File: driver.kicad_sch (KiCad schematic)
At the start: 24 parts, among them U10 74AUC2G32, U11 SN74AUP2G08, U12 74AUC2G32, U13 SN74AUP2G08, U14 74AUC2G32, U15 SN74AUP2G08, U16 SN74AUP2G08, U17 SN74AUP2G08, U18 74AUC2G32, U19 74AUC2G32, U20 SN74AUP2G08, U21 74AUC2G32, U22 SN74AUP2G08, U23 74AUC2G32, U24 SN74AUP2G08, U25 74AUC2G32, U26 SN74AUP2G08, U27 74AUC2G32, U28 SN74AUP2G08, U29 74AUC2G32, U6 Inverter_Schmitt_Dual, U7 Inverter_Schmitt_Dual, U8 SN74AUP2G08, U9 74AUC2G32

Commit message: schem: fix logic error
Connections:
- net D1: now also U26.5
- net ~{D1}: no longer U26.5
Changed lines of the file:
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@@
+	)
+	(junction
+		(at 152.4 77.47)
+		(diameter 0)
+		(color 0 0 0 0)
 	)
 	(junction
@@
 	)
 	(junction
-		(at 156.21 104.14)
-		(diameter 0)
-		(color 0 0 0 0)
-	)
-	(junction
 		(at 26.67 73.66)
 		(diameter 0)
@@
 	(wire
 		(pts
-			(xy 156.21 104.14) (xy 156.21 116.84)
-		)
-		(stroke
-			(width 0)
-			(type default)
-		)
-	)
-	(wire
-		(pts
 			(xy 213.36 21.59) (xy 213.36 20.32)
 		)
@@
 	(wire
 		(pts
-			(xy 156.21 116.84) (xy 173.99 116.84)
-		)
-		(stroke
-			(width 0)
-			(type default)
-		)
-	)
-	(wire
-		(pts
 			(xy 73.66 140.97) (xy 72.39 140.97)
 		)
@@
 	(wire
 		(pts
+			(xy 152.4 77.47) (xy 152.4 116.84)
+		)
+		(stroke
+			(width 0)
+			(type default)
+		)
+	)
+	(wire
+		(pts
 			(xy 233.68 72.39) (xy 234.95 72.39)
 		)
@@
 		)
 		(stroke
+			(width 0)
+			(type default)
+		)
+	)
+	(wire
+		(pts
+			(xy 152.4 116.84) (xy 173.99 116.84)
+		)
+		(stroke

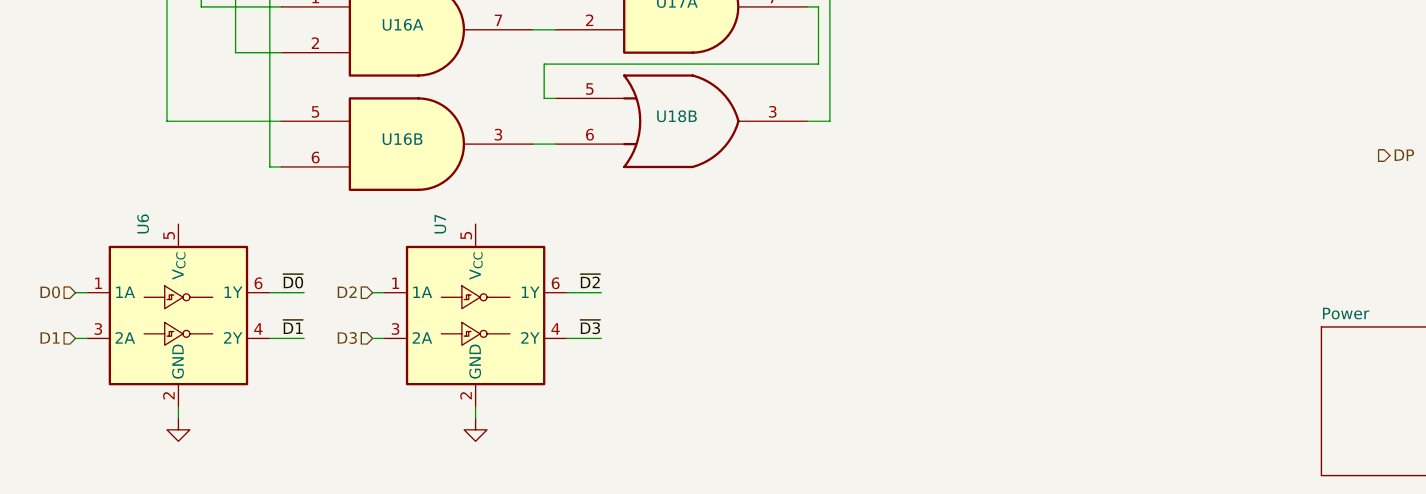
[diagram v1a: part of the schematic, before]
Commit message: schem: add inverters power
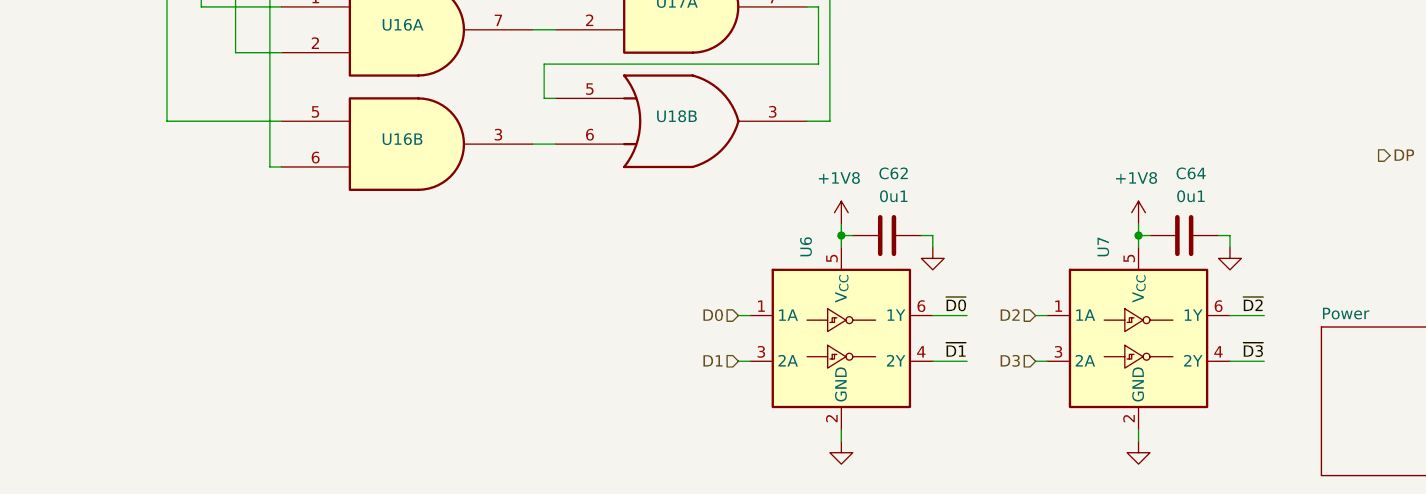
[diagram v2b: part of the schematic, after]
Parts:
- added C62, C64: 0u1, Capacitor_SMD:C_0402_1005Metric, symbol Device:C
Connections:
- net GND: now also C62.2, C64.2
- net +1V8: now reaches U6.5 (V_{CC})
- net +1V8: now also U7.5 (V_{CC}), C62.1, C64.1
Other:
- moved on the sheet: U6, U7

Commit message: schem: run and fix ERC
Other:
- moved on the sheet: U19A
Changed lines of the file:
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@@
 	)
 	(junction
-		(at 116.84 16.51)
-		(diameter 0)
-		(color 0 0 0 0)
-	)
-	(junction
 		(at 83.82 25.4)
 		(diameter 0)
@@
 	)
 	(no_connect
-		(at 144.78 19.05)
+		(at 146.05 19.05)
 	)
 	(no_connect
@@
 	(wire
 		(pts
+			(xy 118.11 16.51) (xy 116.84 16.51)
+		)
+		(stroke
+			(width 0)
+			(type default)
+		)
+	)
+	(wire
+		(pts
 			(xy 152.4 77.47) (xy 152.4 116.84)
 		)
@@
 	(wire
 		(pts
-			(xy 118.11 16.51) (xy 116.84 16.51)
-		)
-		(stroke
-			(width 0)
-			(type default)
-		)
-	)
-	(wire
-		(pts
 			(xy 105.41 168.91) (xy 105.41 170.18)
 		)
@@
 		)
 	)
-	(hierarchical_label "DP"
-		(shape output)
-		(at 165.1 160.02 0)
-		(effects
-			(font
-				(size 1.27 1.27)
-			)
-			(justify left)
-		)
-	)
 	(hierarchical_label "D0"
 		(shape input)
@@
 		)
 	)
-	(hierarchical_label "D3"
-		(shape input)
-		(at 167.64 26.67 90)
-		(effects
-			(font
-				(size 1.27 1.27)
-			)
-			(justify left)
-		)
-	)
 	(hierarchical_label "D1"
 		(shape input)
@@
 	(symbol
 		(lib_id "74xGxx:74AUC2G32")
-		(at 132.08 19.05 0)
+		(at 133.35 19.05 0)
 		(unit 1)
 		(body_style 1)
@@
 		(dnp no)
 		(property "Reference" "U19"
-			(at 130.3131 18.542 0)
+			(at 131.5831 18.542 0)
 			(show_name no)
 			(do_not_autoplace no)
@@
 		)
 		(property "Value" "74AUC2G32"
-			(at 130.81 11.43 0)
+			(at 132.08 11.43 0)
 			(hide yes)
 			(show_name no)
@@
 		)
 		(property "Footprint" "Package_DFN_QFN:QFN-20-1EP_5x5mm_P0.65mm_EP3.35x3.35mm"
-			(at 132.08 19.05 0)
+			(at 133.35 19.05 0)
 			(hide yes)
 			(show_name no)
@@
 		)
 		(property "Datasheet" "http://www.ti.com/lit/sg/scyt129e/scyt129e.pdf"
-			(at 132.08 19.05 0)
+			(at 133.35 19.05 0)
 			(hide yes)
 			(show_name no)
@@
 		)
 		(property "Description" "Dual OR Gate, Low-Voltage CMOS"
-			(at 132.08 19.05 0)
+			(at 133.35 19.05 0)
 			(hide yes)
 			(show_name no)

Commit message: schem: add ordering info to BOM
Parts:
- U10, U12, U14, U18, U19, U21, U23, U25, U27, U29, U9: Basic (none) -> X; JLCPCB Part # (none) -> C2876519; Manufacturer (none) -> Texas Instruments; Manufacturer Part Number (none) -> SN74AUP2G32DCUR
- U11, U13, U15, U16, U17, U20, U22, U24, U26, U28, U8: Basic (none) -> X; JLCPCB Part # (none) -> C544478; Manufacturer (none) -> Texas Instruments; Manufacturer Part Number (none) -> SN74AUP2G08DCUR
- U6, U7: Basic (none) -> X; JLCPCB Part # (none) -> C139318; Manufacturer (none) -> Texas Instruments; Manufacturer Part Number (none) -> SN74AUP2G14DCKR

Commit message: schem: add title
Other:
- company: (none) -> Rémi Ait-Younes
- title: (none) -> DYB Segment Driver 1
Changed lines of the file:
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@@
 	(generator_version "10.0")
 	(paper "A4")
+	(title_block
+		(title "DYB Segment Driver 1")
+		(date "2026-09-29")
+		(rev "01")
+		(company "Rémi Ait-Younes")
+	)
 	(junction
 		(at 144.78 60.96)

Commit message: schem: reannotate
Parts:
- renumbered C62 to C7, C64 to C8, U12 to U10, U14 to U11, U19 to U12, U18 to U13, U10 to U14, U6 to U15, U7 to U16, U20 to U17, U22 to U18, U24 to U19, U26 to U20, U28 to U21, U21 to U22, U25 to U24, U27 to U25, U29 to U26, U8 to U3, U11 to U4, U13 to U5, U15 to U6, U16 to U7, U17 to U8

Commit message: schem: fix footprints
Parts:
- U10, U11, U12, U13, U14, U22, U23, U24, U25, U26, U9: footprint Package_DFN_QFN:QFN-20-1EP_5x5mm_P0.65mm_EP3.35x3.35mm -> Package_SO:VSSOP-8_2.3x2mm_P0.5mm
- U15, U16: footprint Package_TO_SOT_SMD:SOT-23-6 -> Package_TO_SOT_SMD:SOT-363_SC-70-6
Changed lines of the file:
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@@
 			)
 		)
-		(property "Footprint" "Package_TO_SOT_SMD:SOT-23-6"
+		(property "Footprint" "Package_TO_SOT_SMD:SOT-363_SC-70-6"
 			(at 105.41 180.34 0)
 			(hide yes)
@@
 			)
 		)
-		(property "Footprint" "Package_DFN_QFN:QFN-20-1EP_5x5mm_P0.65mm_EP3.35x3.35mm"
+		(property "Footprint" "Package_SO:VSSOP-8_2.3x2mm_P0.5mm"
 			(at 120.65 74.93 0)
 			(hide yes)
@@
 			)
 		)
-		(property "Footprint" "Package_DFN_QFN:QFN-20-1EP_5x5mm_P0.65mm_EP3.35x3.35mm"
+		(property "Footprint" "Package_SO:VSSOP-8_2.3x2mm_P0.5mm"
 			(at 219.71 46.99 0)
 			(hide yes)
@@
 			)
 		)
-		(property "Footprint" "Package_TO_SOT_SMD:SOT-23-6"
+		(property "Footprint" "Package_TO_SOT_SMD:SOT-363_SC-70-6"
 			(at 138.43 180.34 0)
 			(hide yes)
@@
 			)
 		)
-		(property "Footprint" "Package_DFN_QFN:QFN-20-1EP_5x5mm_P0.65mm_EP3.35x3.35mm"
+		(property "Footprint" "Package_SO:VSSOP-8_2.3x2mm_P0.5mm"
 			(at 88.9 77.47 0)
 			(hide yes)
@@
 			)
 		)
-		(property "Footprint" "Package_DFN_QFN:QFN-20-1EP_5x5mm_P0.65mm_EP3.35x3.35mm"
+		(property "Footprint" "Package_SO:VSSOP-8_2.3x2mm_P0.5mm"
 			(at 88.9 127 0)
 			(hide yes)
@@
 			)
 		)
-		(property "Footprint" "Package_DFN_QFN:QFN-20-1EP_5x5mm_P0.65mm_EP3.35x3.35mm"
+		(property "Footprint" "Package_SO:VSSOP-8_2.3x2mm_P0.5mm"
 			(at 120.65 133.35 0)
 			(hide yes)
@@
 			)
 		)
-		(property "Footprint" "Package_DFN_QFN:QFN-20-1EP_5x5mm_P0.65mm_EP3.35x3.35mm"
+		(property "Footprint" "Package_SO:VSSOP-8_2.3x2mm_P0.5mm"
 			(at 219.71 86.36 0)
 			(hide yes)
@@
 			)
 		)
-		(property "Footprint" "Package_DFN_QFN:QFN-20-1EP_5x5mm_P0.65mm_EP3.35x3.35mm"
+		(property "Footprint" "Package_SO:VSSOP-8_2.3x2mm_P0.5mm"
 			(at 250.19 74.93 0)
 			(hide yes)
@@
 			)
 		)
-		(property "Footprint" "Package_DFN_QFN:QFN-20-1EP_5x5mm_P0.65mm_EP3.35x3.35mm"
+		(property "Footprint" "Package_SO:VSSOP-8_2.3x2mm_P0.5mm"
 			(at 119.38 96.52 0)
 			(hide yes)
@@
 			)
 		)
-		(property "Footprint" "Package_DFN_QFN:QFN-20-1EP_5x5mm_P0.65mm_EP3.35x3.35mm"
+		(property "Footprint" "Package_SO:VSSOP-8_2.3x2mm_P0.5mm"
 			(at 88.9 36.83 0)
 			(hide yes)
@@
 			)
 		)
-		(property "Footprint" "Package_DFN_QFN:QFN-20-1EP_5x5mm_P0.65mm_EP3.35x3.35mm"
+		(property "Footprint" "Package_SO:VSSOP-8_2.3x2mm_P0.5mm"
 			(at 219.71 64.77 0)
 			(hide yes)
@@
 			)
 		)
-		(property "Footprint" "Package_DFN_QFN:QFN-20-1EP_5x5mm_P0.65mm_EP3.35x3.35mm"
+		(property "Footprint" "Package_SO:VSSOP-8_2.3x2mm_P0.5mm"
 			(at 88.9 49.53 0)
 			(hide yes)
@@
 			)
 		)
-		(property "Footprint" "Package_DFN_QFN:QFN-20-1EP_5x5mm_P0.65mm_EP3.35x3.35mm"
+		(property "Footprint" "Package_SO:VSSOP-8_2.3x2mm_P0.5mm"
 			(at 219.71 109.22 0)
 			(hide yes)
@@
 			)
 		)
-		(property "Footprint" "Package_DFN_QFN:QFN-20-1EP_5x5mm_P0.65mm_EP3.35x3.35mm"
+		(property "Footprint" "Package_SO:VSSOP-8_2.3x2mm_P0.5mm"
 			(at 88.9 104.14 0)
 			(hide yes)
@@
 			)
 		)
-		(property "Footprint" "Package_DFN_QFN:QFN-20-1EP_5x5mm_P0.65mm_EP3.35x3.35mm"
+		(property "Footprint" "Package_SO:VSSOP-8_2.3x2mm_P0.5mm"
 			(at 270.51 19.05 0)
 			(hide yes)
@@
 			)
 		)
-		(property "Footprint" "Package_DFN_QFN:QFN-20-1EP_5x5mm_P0.65mm_EP3.35x3.35mm"
+		(property "Footprint" "Package_SO:VSSOP-8_2.3x2mm_P0.5mm"
 			(at 133.35 19.05 0)
 			(hide yes)
@@
 			)
 		)
-		(property "Footprint" "Package_DFN_QFN:QFN-20-1EP_5x5mm_P0.65mm_EP3.35x3.35mm"
+		(property "Footprint" "Package_SO:VSSOP-8_2.3x2mm_P0.5mm"
 			(at 250.19 116.84 0)
 			(hide yes)
@@
 			)
 		)
-		(property "Footprint" "Package_DFN_QFN:QFN-20-1EP_5x5mm_P0.65mm_EP3.35x3.35mm"
+		(property "Footprint" "Package_SO:VSSOP-8_2.3x2mm_P0.5mm"
 			(at 88.9 156.21 0)
 			(hide yes)
@@
 			)
 		)
-		(property "Footprint" "Package_DFN_QFN:QFN-20-1EP_5x5mm_P0.65mm_EP3.35x3.35mm"
+		(property "Footprint" "Package_SO:VSSOP-8_2.3x2mm_P0.5mm"
 			(at 119.38 43.18 0)
 			(hide yes)
@@
 			)
 		)
-		(property "Footprint" "Package_DFN_QFN:QFN-20-1EP_5x5mm_P0.65mm_EP3.35x3.35mm"
+		(property "Footprint" "Package_SO:VSSOP-8_2.3x2mm_P0.5mm"
 			(at 231.14 33.02 0)
 			(hide yes)
@@
 			)
 		)
-		(property "Footprint" "Package_DFN_QFN:QFN-20-1EP_5x5mm_P0.65mm_EP3.35x3.35mm"
+		(property "Footprint" "Package_SO:VSSOP-8_2.3x2mm_P0.5mm"
 			(at 196.85 19.05 0)
 			(hide yes)
@@
 			)
 		)
-		(property "Footprint" "Package_DFN_QFN:QFN-20-1EP_5x5mm_P0.65mm_EP3.35x3.35mm"
+		(property "Footprint" "Package_SO:VSSOP-8_2.3x2mm_P0.5mm"
 			(at 100.33 22.86 0)
 			(hide yes)
@@
 			)
 		)
-		(property "Footprint" "Package_DFN_QFN:QFN-20-1EP_5x5mm_P0.65mm_EP3.35x3.35mm"
+		(property "Footprint" "Package_SO:VSSOP-8_2.3x2mm_P0.5mm"
 			(at 219.71 125.73 0)
 			(hide yes)

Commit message: schem: swap inverter channels
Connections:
- net D0: now also U15.3 (2A); no longer U15.1 (1A)
- net D1: now also U15.1 (1A); no longer U15.3 (2A)
- net D2: now also U16.3 (2A); no longer U16.1 (1A)
- net D3: now also U16.1 (1A); no longer U16.3 (2A)
- net ~{D0}: now also U15.4 (2Y); no longer U15.6 (1Y)
- net ~{D1}: now also U15.6 (1Y); no longer U15.4 (2Y)
- net ~{D2}: now also U16.4 (2Y); no longer U16.6 (1Y)
- net ~{D3}: now also U16.6 (1Y); no longer U16.4 (2Y)
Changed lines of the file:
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@@
+		)
+	)
+	(label "~{D3}"
+		(at 152.4 177.8 180)
+		(effects
+			(font
+				(size 1.27 1.27)
+			)
+			(justify right bottom)
+		)
+	)
+	(label "~{D0}"
+		(at 119.38 182.88 180)
+		(effects
+			(font
+				(size 1.27 1.27)
+			)
+			(justify right bottom)
 		)
 	)
@@
 	)
 	(label "~{D1}"
+		(at 119.38 177.8 180)
+		(effects
+			(font
+				(size 1.27 1.27)
+			)
+			(justify right bottom)
+		)
+	)
+	(label "~{D1}"
 		(at 24.13 26.67 0)
 		(effects
@@
 		)
 	)
-	(label "~{D1}"
-		(at 119.38 182.88 180)
-		(effects
-			(font
-				(size 1.27 1.27)
-			)
-			(justify right bottom)
-		)
-	)
-	(label "~{D0}"
-		(at 119.38 177.8 180)
+	(label "~{D2}"
+		(at 152.4 182.88 180)
 		(effects
 			(font
@@
 		)
 	)
-	(label "~{D3}"
-		(at 152.4 182.88 180)
-		(effects
-			(font
-				(size 1.27 1.27)
-			)
-			(justify right bottom)
-		)
-	)
-	(label "~{D2}"
-		(at 152.4 177.8 180)
-		(effects
-			(font
-				(size 1.27 1.27)
-			)
-			(justify right bottom)
-		)
-	)
 	(label "~{D2}"
 		(at 31.75 26.67 0)
@@
 		)
 	)
+	(hierarchical_label "D3"
+		(shape input)
+		(at 127 177.8 180)
+		(effects
+			(font
+				(size 1.27 1.27)
+			)
+			(justify right)
+		)
+	)
 	(hierarchical_label "B"
 		(shape output)
@@
 		)
 	)
+	(hierarchical_label "D1"
+		(shape input)
+		(at 93.98 177.8 180)
+		(effects
+			(font
+				(size 1.27 1.27)
+			)
+			(justify right)
+		)
+	)
 	(hierarchical_label "D"
 		(shape output)
@@
 		)
 	)
+	(hierarchical_label "D2"
+		(shape input)
+		(at 30.48 26.67 90)
+		(effects
+			(font
+				(size 1.27 1.27)
+			)
+			(justify left)
+		)
+	)
+	(hierarchical_label "D1"
+		(shape input)
+		(at 22.86 26.67 90)
+		(effects
+			(font
+				(size 1.27 1.27)
+			)
+			(justify left)
+		)
+	)
+	(hierarchical_label "G"
+		(shape output)
+		(at 264.16 116.84 0)
+		(effects
+			(font
+				(size 1.27 1.27)
+			)
+			(justify left)
+		)
+	)
 	(hierarchical_label "D0"
 		(shape input)
-		(at 93.98 177.8 180)
-		(effects
-			(font
-				(size 1.27 1.27)
-			)
-			(justify right)
+		(at 93.98 182.88 180)
+		(effects
+			(font
+				(size 1.27 1.27)
+			)
+			(justify right)
+		)
+	)
+	(hierarchical_label "F"
+		(shape output)
+		(at 264.16 74.93 0)
+		(effects
+			(font
+				(size 1.27 1.27)
+			)
+			(justify left)
+		)
+	)
+	(hierarchical_label "D3"
+		(shape input)
+		(at 38.1 26.67 90)
+		(effects
+			(font
+				(size 1.27 1.27)
+			)
+			(justify left)
 		)
 	)
 	(hierarchical_label "D2"
 		(shape input)
-		(at 30.48 26.67 90)
-		(effects
-			(font
-				(size 1.27 1.27)
-			)
-			(justify left)
-		)
-	)
-	(hierarchical_label "D1"
-		(shape input)
-		(at 22.86 26.67 90)
-		(effects
-			(font
-				(size 1.27 1.27)
-			)
-			(justify left)
-		)
-	)
-	(hierarchical_label "G"
-		(shape output)
-		(at 264.16 116.84 0)
-		(effects
-			(font
-				(size 1.27 1.27)
-			)
-			(justify left)
-		)
-	)
-	(hierarchical_label "F"
-		(shape output)
-		(at 264.16 74.93 0)
-		(effects
-			(font
-				(size 1.27 1.27)
-			)
-			(justify left)
-		)
-	)
-	(hierarchical_label "D3"
-		(shape input)
-		(at 38.1 26.67 90)
-		(effects
-			(font
-				(size 1.27 1.27)
-			)
-			(justify left)
-		)
-	)
-	(hierarchical_label "D3"
+		(at 160.02 26.67 90)
+		(effects
+			(font
+				(size 1.27 1.27)
+			)
+			(justify left)
+		)
+	)
+	(hierarchical_label "D0"
+		(shape input)
+		(at 15.24 26.67 90)
+		(effects
+			(font
+				(size 1.27 1.27)
+			)
+			(justify left)
+		)
+	)
+	(hierarchical_label "E"
+		(shape output)
+		(at 233.68 46.99 0)
+		(effects
+			(font
+				(size 1.27 1.27)
+			)
+			(justify left)
+		)
+	)
+	(hierarchical_label "D0"
+		(shape input)
+		(at 144.78 26.67 90)
+		(effects
+			(font
+				(size 1.27 1.27)
+			)
+			(justify left)
+		)
+	)
+	(hierarchical_label "D2"
 		(shape input)
 		(at 127 182.88 180)
@@
 		)
 	)
-	(hierarchical_label "D2"
-		(shape input)
-		(at 160.02 26.67 90)
-		(effects
-			(font
-				(size 1.27 1.27)
-			)
-			(justify left)
-		)
-	)
-	(hierarchical_label "D0"
-		(shape input)
-		(at 15.24 26.67 90)
-		(effects
-			(font
-				(size 1.27 1.27)
-			)
-			(justify left)
-		)
-	)
-	(hierarchical_label "D1"
-		(shape input)
-		(at 93.98 182.88 180)
-		(effects
-			(font
-				(size 1.27 1.27)
-			)
-			(justify right)
-		)
-	)
-	(hierarchical_label "D2"
-		(shape input)
-		(at 127 177.8 180)
-		(effects
-			(font
-				(size 1.27 1.27)
-			)
-			(justify right)
-		)
-	)
-	(hierarchical_label "E"
-		(shape output)
-		(at 233.68 46.99 0)
-		(effects
-			(font
-				(size 1.27 1.27)
-			)
-			(justify left)
-		)
-	)
-	(hierarchical_label "D0"
-		(shape input)
-		(at 144.78 26.67 90)
-		(effects
-			(font
-				(size 1.27 1.27)
-			)
-			(justify left)
-		)
-	)
